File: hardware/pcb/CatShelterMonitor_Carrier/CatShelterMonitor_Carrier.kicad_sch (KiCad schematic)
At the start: 8 parts, among them J1 Conn_01x06

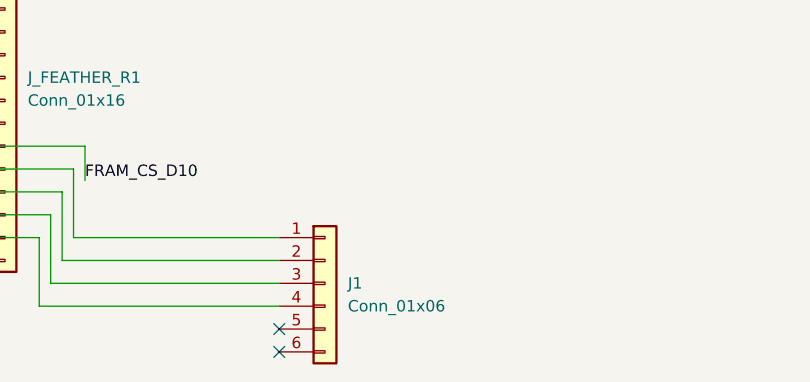
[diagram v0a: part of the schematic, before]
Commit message: Carrier PCB: Feather header spacing fixed, routing reconnected, DRC clean
Baseline commit before board size reduction.
Feather headers set to exact 20.32mm spacing and locked.
All nets routed, GND pour complete, DRC clean.
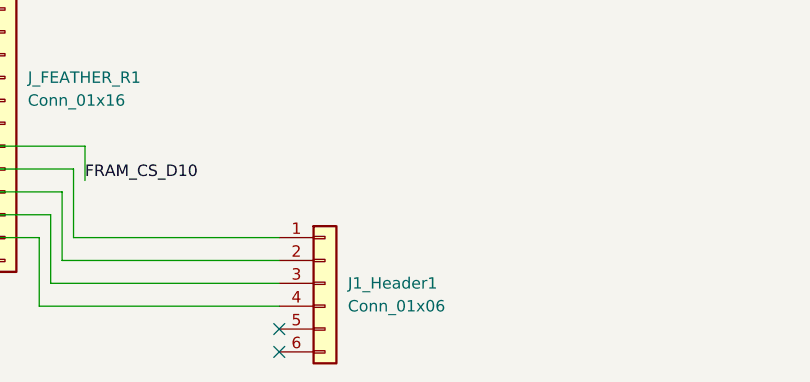
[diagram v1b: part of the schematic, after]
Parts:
- J1_Header1: renamed from J1; footprint (none) -> Connector_PinSocket_2.54mm:PinSocket_1x06_P2.54mm_Vertical
- J_FEATHER_L1, J_FEATHER_R1: footprint (none) -> Connector_PinSocket_2.54mm:PinSocket_1x16_P2.54mm_Vertical
- J_FRAM1: footprint (none) -> Connector_PinSocket_2.54mm:PinSocket_1x09_P2.54mm_Vertical
- J_PROBE_1, J_PROBE_2: footprint (none) -> TerminalBlock_4Ucon:TerminalBlock_4Ucon_1x03_P3.50mm_Vertical
- J_RTC1: footprint (none) -> Connector_PinSocket_2.54mm:PinSocket_1x08_P2.54mm_Vertical
- R_PULLUP_A1: footprint (none) -> Resistor_THT:R_Axial_DIN0207_L6.3mm_D2.5mm_P7.62mm_Horizontal
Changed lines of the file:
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@@
 		(on_board yes)
 		(dnp no)
-		(property "Reference" "#PWR08"
+		(property "Reference" "#PWR07"
 			(at 222.25 72.39 0)
 			(effects
@@
 			(project "CatShelterMonitor_Carrier"
 				(path "/c4b0c962-af87-494a-9ee2-529dcd2c58b2"
-					(reference "#PWR08")
+					(reference "#PWR07")
 					(unit 1)
 				)
@@
 		(on_board yes)
 		(dnp no)
-		(property "Reference" "#PWR06"
+		(property "Reference" "#PWR01"
 			(at 198.12 25.4 0)
 			(effects
@@
 			(project "CatShelterMonitor_Carrier"
 				(path "/c4b0c962-af87-494a-9ee2-529dcd2c58b2"
-					(reference "#PWR06")
+					(reference "#PWR01")
 					(unit 1)
 				)
@@
 			)
 		)
-		(property "Footprint" ""
+		(property "Footprint" "Connector_PinSocket_2.54mm:PinSocket_1x16_P2.54mm_Vertical"
 			(at 92.71 96.52 0)
 			(effects
@@
 		(on_board yes)
 		(dnp no)
-		(property "Reference" "#PWR05"
+		(property "Reference" "#PWR02"
 			(at 144.78 34.29 0)
 			(effects
@@
 			(project "CatShelterMonitor_Carrier"
 				(path "/c4b0c962-af87-494a-9ee2-529dcd2c58b2"
-					(reference "#PWR05")
+					(reference "#PWR02")
 					(unit 1)
 				)
@@
 		(on_board yes)
 		(dnp no)
-		(property "Reference" "#PWR02"
+		(property "Reference" "#PWR03"
 			(at 36.83 41.91 0)
 			(effects
@@
 			(project ""
 				(path "/c4b0c962-af87-494a-9ee2-529dcd2c58b2"
-					(reference "#PWR02")
+					(reference "#PWR03")
 					(unit 1)
 				)
@@
 		(dnp no)
 		(fields_autoplaced yes)
-		(property "Reference" "J1"
+		(property "Reference" "J1_Header1"
 			(at 157.48 119.3799 0)
 			(effects
@@
 			)
 		)
-		(property "Footprint" ""
+		(property "Footprint" "Connector_PinSocket_2.54mm:PinSocket_1x06_P2.54mm_Vertical"
 			(at 154.94 119.38 0)
 			(effects
@@
 			(project ""
 				(path "/c4b0c962-af87-494a-9ee2-529dcd2c58b2"
-					(reference "J1")
+					(reference "J1_Header1")
 					(unit 1)
 				)
@@
 		(on_board yes)
 		(dnp no)
-		(property "Reference" "#PWR07"
+		(property "Reference" "#PWR04"
 			(at 196.85 52.07 0)
 			(effects
@@
 			(project "CatShelterMonitor_Carrier"
 				(path "/c4b0c962-af87-494a-9ee2-529dcd2c58b2"
-					(reference "#PWR07")
+					(reference "#PWR04")
 					(unit 1)
 				)
@@
 		(dnp no)
 		(fields_autoplaced yes)
-		(property "Reference" "#PWR01"
+		(property "Reference" "#PWR06"
 			(at 36.83 57.15 0)
 			(effects
@@
 			(project ""
 				(path "/c4b0c962-af87-494a-9ee2-529dcd2c58b2"
-					(reference "#PWR01")
+					(reference "#PWR06")
 					(unit 1)
 				)
@@
 			)
 		)
-		(property "Footprint" ""
+		(property "Footprint" "TerminalBlock_4Ucon:TerminalBlock_4Ucon_1x03_P3.50mm_Vertical"
 			(at 210.82 54.61 0)
 			(effects
@@
 			)
 		)
-		(property "Footprint" ""
+		(property "Footprint" "Connector_PinSocket_2.54mm:PinSocket_1x09_P2.54mm_Vertical"
 			(at 105.41 46.99 0)
 			(effects
@@
 			)
 		)
-		(property "Footprint" ""
+		(property "Footprint" "Resistor_THT:R_Axial_DIN0207_L6.3mm_D2.5mm_P7.62mm_Horizontal"
 			(at 172.212 69.85 90)
 			(effects
@@
 			)
 		)
-		(property "Footprint" ""
+		(property "Footprint" "TerminalBlock_4Ucon:TerminalBlock_4Ucon_1x03_P3.50mm_Vertical"
 			(at 210.82 36.83 0)
 			(effects
@@
 			)
 		)
-		(property "Footprint" ""
+		(property "Footprint" "Connector_PinSocket_2.54mm:PinSocket_1x16_P2.54mm_Vertical"
 			(at 119.38 96.52 0)
 			(effects
@@
 			)
 		)
-		(property "Footprint" ""
+		(property "Footprint" "Connector_PinSocket_2.54mm:PinSocket_1x08_P2.54mm_Vertical"
 			(at 156.21 41.91 0)
 			(effects
@@
 		(on_board yes)
 		(dnp no)
-		(property "Reference" "#PWR04"
+		(property "Reference" "#PWR05"
 			(at 76.2 53.34 0)
 			(effects
@@
 			(project "CatShelterMonitor_Carrier"
 				(path "/c4b0c962-af87-494a-9ee2-529dcd2c58b2"
-					(reference "#PWR04")
+					(reference "#PWR05")
 					(unit 1)
 				)
@@
 		(on_board yes)
 		(dnp no)
-		(property "Reference" "#PWR03"
+		(property "Reference" "#PWR08"
 			(at 74.93 83.82 0)
 			(effects
@@
 			(project "CatShelterMonitor_Carrier"
 				(path "/c4b0c962-af87-494a-9ee2-529dcd2c58b2"
-					(reference "#PWR03")
-					(unit 1)
-				)
+					(reference "#PWR08")
+					(unit 1)
+				)

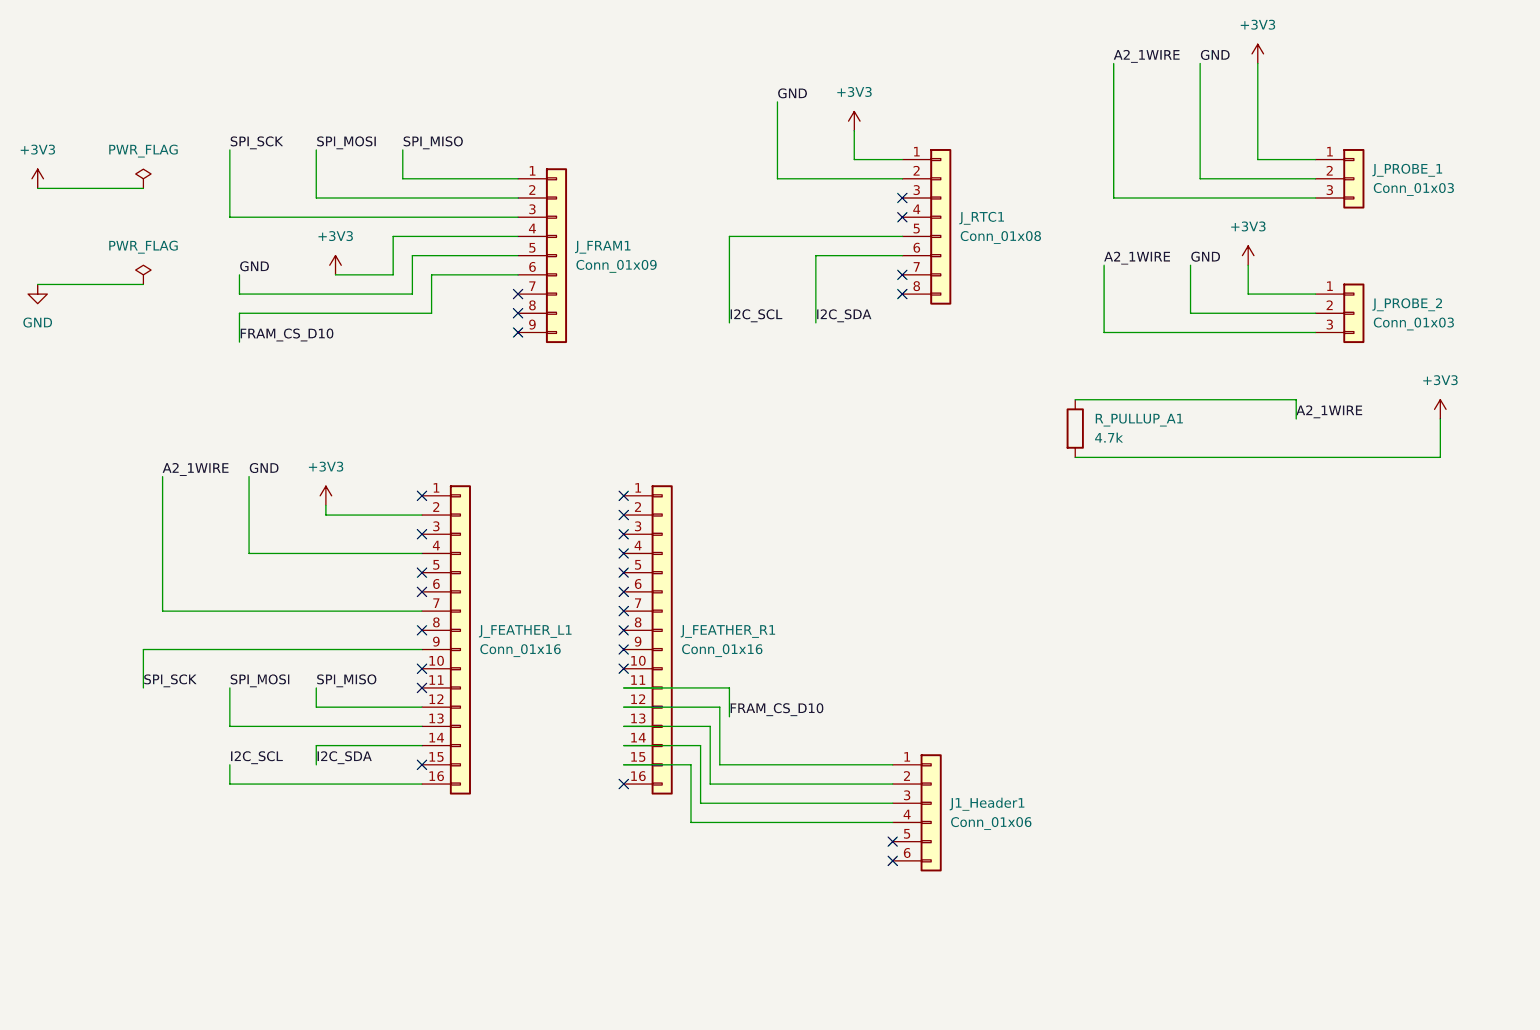
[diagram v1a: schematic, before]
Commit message: Resolve footprint parity errors and verify probe routing
Corrected Schematic Parity: Updated J_PROBE_1 and J_PROBE_2 symbols to match the assigned TerminalBlock_4Ucon footprints.

Modified Symbol Library: Updated the footprint filters in Project_Connectors.kicad_sym to allow TerminalBlock* footprints, resolving persistent DRC warnings.

Verified Board Connectivity: Ran a full Design Rules Check (DRC) confirming zero violations and zero unconnected items across all nets.

Synchronized Project Files: Linked schematic values and footprints to the PCB layout using the "Update PCB from Schematic" tool with re-linking enabled.
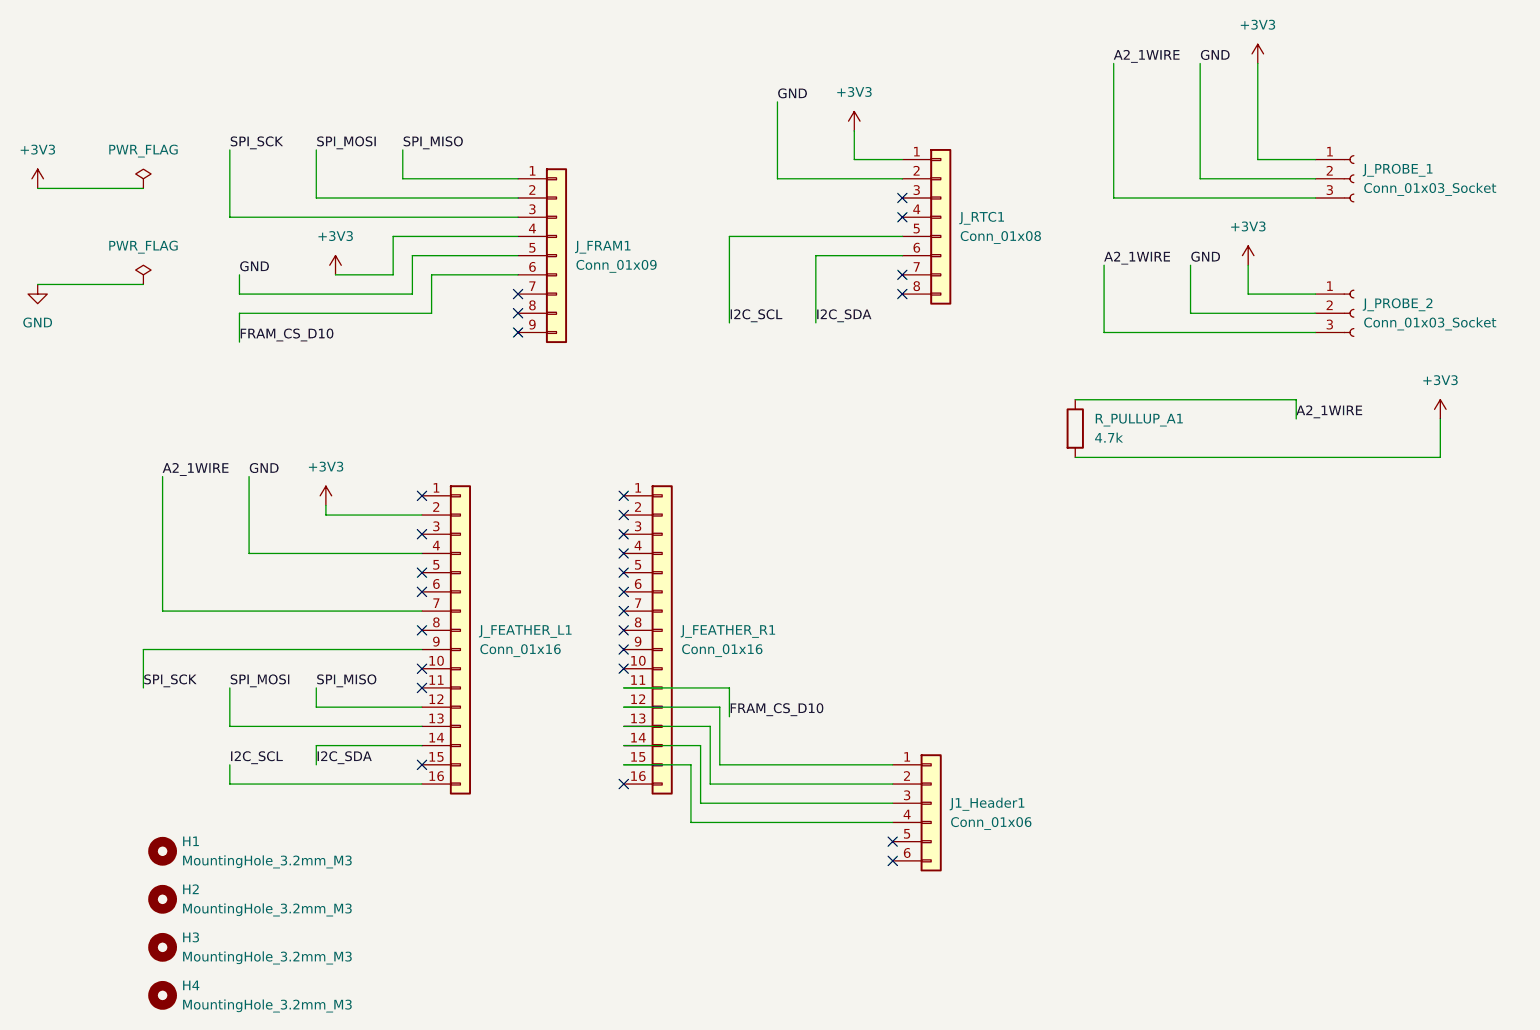
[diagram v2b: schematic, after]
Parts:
- removed J_PROBE_1, J_PROBE_2: Conn_01x03, TerminalBlock_4Ucon:TerminalBlock_4Ucon_1x03_P3.50mm_Vertical, symbol Connector_Generic:Conn_01x03
- added H1, H2, H3, H4: MountingHole_3.2mm_M3, MountingHole:MountingHole_3.2mm_M3, symbol Mechanical:MountingHole
- added J_PROBE_1, J_PROBE_2: Conn_01x03_Socket, TerminalBlock_4Ucon:TerminalBlock_4Ucon_1x03_P3.50mm_Vertical, symbol Connector:Conn_01x03_Socket
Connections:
- net +3V3: now also J_PROBE_1.1 (Pin_1), J_PROBE_2.1 (Pin_1)
- net A2_1WIRE: now also J_PROBE_1.3 (Pin_3), J_PROBE_2.3 (Pin_3)
- net GND: now also J_PROBE_1.2 (Pin_2), J_PROBE_2.2 (Pin_2)
